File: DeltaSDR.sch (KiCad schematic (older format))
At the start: 48 parts, among them J1 Conn_01x03_Male, J2 Conn_01x05_Male, J3 Barrel_Jack, J4 USB_A, U1 TC1262-33, U2 Si570, U4 PCM3060, U5 CY8C3246PVI-147, U6 TLV761, U7 TLV761, U8 74HC74, Y1 Crystal

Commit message: Added RF front end and LNA
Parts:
- C1, C10, C11, C12, C13, C14, C15, C16, C17, C18, C19, C2, C20, C21, C22, C23, C24, C3, C4, C5, C6, C7, C8, C9: symbol DeltaSDR-rescue:C-Device -> DeltaSDR-rescue:C-Device-DeltaSDR-rescue
- D1: symbol DeltaSDR-rescue:LED-Device -> DeltaSDR-rescue:LED-Device-DeltaSDR-rescue
- D2: symbol device:D -> DeltaSDR-rescue:D-device
- D3: symbol ESD_Protection:PRTR5V0U2X -> DeltaSDR-rescue:PRTR5V0U2X-ESD_Protection
- J3: symbol Connector:Barrel_Jack -> DeltaSDR-rescue:Barrel_Jack-Connector
- L1: symbol device:L -> DeltaSDR-rescue:L-device
- R1, R2, R3, R4, R5, R6, R7, R8: symbol DeltaSDR-rescue:R-Device -> DeltaSDR-rescue:R-Device-DeltaSDR-rescue
- U1: symbol regul:TC1262-33 -> DeltaSDR-rescue:TC1262-33-regul
- U2: symbol DeltaSDR-rescue:Si570-Oscillator -> DeltaSDR-rescue:Si570-Oscillator-DeltaSDR-rescue
- U4: symbol DeltaSDR-rescue:PCM3060-riske-symbols -> DeltaSDR-rescue:PCM3060-riske-symbols-DeltaSDR-rescue
- U5: symbol DeltaSDR-rescue:CY8C3246PVI-147-cy8c3246pvi-147 -> DeltaSDR-rescue:CY8C3246PVI-147-cy8c3246pvi-147-DeltaSDR-rescue
- U6, U7: symbol MLAB_U:LM1117 -> DeltaSDR-rescue:LM1117-MLAB_U
- U8: symbol Logic_74xx:74HC74 -> DeltaSDR-rescue:74HC74-Logic_74xx
- Y1: symbol DeltaSDR-rescue:Crystal-Device -> DeltaSDR-rescue:Crystal-Device-DeltaSDR-rescue
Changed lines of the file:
@@
 EESchema Schematic File Version 4
-EELAYER 30 0
+LIBS:DeltaSDR-cache
+EELAYER 29 0
 EELAYER END
 $Descr A4 11693 8268
@@
 $EndDescr
 $Comp
-L DeltaSDR-rescue:Si570-Oscillator U2
+L DeltaSDR-rescue:Si570-Oscillator-DeltaSDR-rescue U2
 U 1 1 5E8B430C
 P 2000 2725
@@
 $EndComp
 $Comp
-L DeltaSDR-rescue:CY8C3246PVI-147-cy8c3246pvi-147 U5
+L DeltaSDR-rescue:CY8C3246PVI-147-cy8c3246pvi-147-DeltaSDR-rescue U5
 U 1 1 5E8B959A
 P 8100 4000
@@
 $EndComp
 $Comp
-L DeltaSDR-rescue:PCM3060-riske-symbols U4
+L DeltaSDR-rescue:PCM3060-riske-symbols-DeltaSDR-rescue U4
 U 1 1 5E8BE1D1
 P 3400 4450
@@
 $EndComp
 $Comp
-L DeltaSDR-rescue:C-Device C5
+L DeltaSDR-rescue:C-Device-DeltaSDR-rescue C5
 U 1 1 5E8BF4A8
 P 9500 3050
@@
 Connection ~ 9500 2850
 $Comp
-L DeltaSDR-rescue:C-Device C2
+L DeltaSDR-rescue:C-Device-DeltaSDR-rescue C2
 U 1 1 5E8C2E1C
 P 9100 3150
@@
 	9100 3300 9100 3350
 $Comp
-L DeltaSDR-rescue:C-Device C6
+L DeltaSDR-rescue:C-Device-DeltaSDR-rescue C6
 U 1 1 5E8C4103
 P 9700 3750
@@
 XTALo
 $Comp
-L DeltaSDR-rescue:C-Device C4
+L DeltaSDR-rescue:C-Device-DeltaSDR-rescue C4
 U 1 1 5E8C8B8E
 P 9400 4050
@@
 Vccd
 $Comp
-L DeltaSDR-rescue:C-Device C1
+L DeltaSDR-rescue:C-Device-DeltaSDR-rescue C1
 U 1 1 5E8D021E
 P 9000 4250
@@
 BOOT
 $Comp
-L DeltaSDR-rescue:C-Device C3
+L DeltaSDR-rescue:C-Device-DeltaSDR-rescue C3
 U 1 1 5E8D2DEC
 P 9200 4750
@@
 AMP
 $Comp
-L DeltaSDR-rescue:LED-Device D1
+L DeltaSDR-rescue:LED-Device-DeltaSDR-rescue D1
 U 1 1 5E8D990B
 P 7150 4550
@@
 $EndComp
 $Comp
-L DeltaSDR-rescue:R-Device R3
+L DeltaSDR-rescue:R-Device-DeltaSDR-rescue R3
 U 1 1 5E8DA7CD
 P 6700 4550
@@
 	7450 4550 7550 4550
 $Comp
-L DeltaSDR-rescue:C-Device C14
+L DeltaSDR-rescue:C-Device-DeltaSDR-rescue C14
 U 1 1 5E8DDA4D
 P 6850 4100
@@
 	7300 4550 7450 4550
 $Comp
-L DeltaSDR-rescue:C-Device C11
+L DeltaSDR-rescue:C-Device-DeltaSDR-rescue C11
 U 1 1 5E8E3DCC
 P 6550 3850
@@
 LRCK1
 $Comp
-L DeltaSDR-rescue:C-Device C13
+L DeltaSDR-rescue:C-Device-DeltaSDR-rescue C13
 U 1 1 5E8F24C0
 P 6850 3200
@@
 BCK1
 $Comp
-L DeltaSDR-rescue:C-Device C9
+L DeltaSDR-rescue:C-Device-DeltaSDR-rescue C9
 U 1 1 5E8FBE37
 P 4650 4400
@@
 SCL
 $Comp
-L DeltaSDR-rescue:C-Device C8
+L DeltaSDR-rescue:C-Device-DeltaSDR-rescue C8
 U 1 1 5E915664
 P 2050 4600
@@
 Connection ~ 2050 4400
 $Comp
-L DeltaSDR-rescue:R-Device R1
+L DeltaSDR-rescue:R-Device-DeltaSDR-rescue R1
 U 1 1 5E93592F
 P 4450 7100
@@
 $EndComp
 $Comp
-L DeltaSDR-rescue:R-Device R2
+L DeltaSDR-rescue:R-Device-DeltaSDR-rescue R2
 U 1 1 5E935C48
 P 4800 7100
@@
 BOOT jumper \n1-2 enables USB bootloader.\n2-3 for normal operation
 $Comp
-L DeltaSDR-rescue:Crystal-Device Y1
+L DeltaSDR-rescue:Crystal-Device-DeltaSDR-rescue Y1
 U 1 1 5E94EC07
 P 6550 5200
@@
 $EndComp
 $Comp
-L DeltaSDR-rescue:C-Device C10
+L DeltaSDR-rescue:C-Device-DeltaSDR-rescue C10
 U 1 1 5E94F97D
 P 6300 5400
@@
 $EndComp
 $Comp
-L DeltaSDR-rescue:C-Device C12
+L DeltaSDR-rescue:C-Device-DeltaSDR-rescue C12
 U 1 1 5E950325
 P 6800 5400
@@
 NoConn ~ 2500 2825
 $Comp
-L DeltaSDR-rescue:C-Device C7
+L DeltaSDR-rescue:C-Device-DeltaSDR-rescue C7
 U 1 1 5E981D93
 P 1150 2425
@@
 $EndSheet
 $Comp
-L regul:TC1262-33 U1
+L DeltaSDR-rescue:TC1262-33-regul U1
 U 1 1 5E8E4808
 P 6675 950
@@
 $EndComp
 $Comp
-L DeltaSDR-rescue:C-Device C22
+L DeltaSDR-rescue:C-Device-DeltaSDR-rescue C22
 U 1 1 5E8E4DAA
 P 7025 1150
@@
 	7025 950  7025 1000
 $Comp
-L DeltaSDR-rescue:C-Device C21
+L DeltaSDR-rescue:C-Device-DeltaSDR-rescue C21
 U 1 1 5E8F2026
 P 6225 1150
@@
 	6225 1300 6225 1350
 $Comp
-L mdSupply:+5V #PWR0143
+L DeltaSDR-rescue:+5V-mdSupply #PWR0143
 U 1 1 5E8FB0F8
 P 6225 775
@@
 Connection ~ 7025 950
 $Comp
-L Connector:Barrel_Jack J3
+L DeltaSDR-rescue:Barrel_Jack-Connector J3
 U 1 1 5E905C03
 P 1075 1050
@@
 $EndComp
 $Comp
-L device:D D2
+L DeltaSDR-rescue:D-device D2
 U 1 1 5E907521
 P 1650 950
@@
 	1375 950  1500 950
 $Comp
-L DeltaSDR-rescue:C-Device C16
+L DeltaSDR-rescue:C-Device-DeltaSDR-rescue C16
 U 1 1 5E915B7F
 P 1825 1150
@@
 	1425 1150 1425 1325
 $Comp
-L device:L L1
+L DeltaSDR-rescue:L-device L1
 U 1 1 5E92544F
 P 2050 950
@@
 $EndComp
 $Comp
-L DeltaSDR-rescue:C-Device C15
+L DeltaSDR-rescue:C-Device-DeltaSDR-rescue C15
 U 1 1 5E925F10
 P 2275 1125
@@
 	2275 1275 2275 1325
 $Comp
-L Logic_74xx:74HC74 U8
+L DeltaSDR-rescue:74HC74-Logic_74xx U8
 U 1 1 5E9675F6
 P 3150 2725
@@
 $EndComp
 $Comp
-L Logic_74xx:74HC74 U8
+L DeltaSDR-rescue:74HC74-Logic_74xx U8
 U 2 1 5E9682AE
 P 4025 2725
@@
 $EndComp
 $Comp
-L Logic_74xx:74HC74 U8
+L DeltaSDR-rescue:74HC74-Logic_74xx U8
 U 3 1 5E9696A3
 P 5025 2625
@@
 $EndComp
 $Comp
-L DeltaSDR-rescue:C-Device C24
+L DeltaSDR-rescue:C-Device-DeltaSDR-rescue C24
 U 1 1 5E96B520
 P 5375 2625
@@
 Connection ~ 5025 3050
 $Comp
-L mdSupply:+5V #PWR0152
+L DeltaSDR-rescue:+5V-mdSupply #PWR0152
 U 1 1 5E97E791
 P 5025 2125
@@
 	2700 2725 2850 2725
 $Comp
-L mdSupply:+5V #PWR0153
+L DeltaSDR-rescue:+5V-mdSupply #PWR0153
 U 1 1 5EA064BB
 P 4200 2350
@@
 $EndComp
 $Comp
-L ESD_Protection:PRTR5V0U2X D3
+L DeltaSDR-rescue:PRTR5V0U2X-ESD_Protection D3
 U 1 1 5EA126D7
 P 2925 6075
@@
 	3225 6775 2400 6775
 $Comp
-L DeltaSDR-rescue:R-Device R8
+L DeltaSDR-rescue:R-Device-DeltaSDR-rescue R8
 U 1 1 5EA3C1AA
 P 2000 7275
@@
 	2050 7450 2000 7450
 $Comp
-L DeltaSDR-rescue:R-Device R6
+L DeltaSDR-rescue:R-Device-DeltaSDR-rescue R6
 U 1 1 5EA5D9BB
 P 3500 6675
@@
 $EndComp
 $Comp
-L DeltaSDR-rescue:R-Device R7
+L DeltaSDR-rescue:R-Device-DeltaSDR-rescue R7
 U 1 1 5EA5EDBA
 P 3500 6775
@@
 USB-
 $Comp
-L MLAB_U:LM1117 U6
+L DeltaSDR-rescue:LM1117-MLAB_U U6
 U 1 1 5EA8F70D
 P 3000 1050
@@
 	3000 1350 3000 1375
 $Comp
-L DeltaSDR-rescue:C-Device C17
+L DeltaSDR-rescue:C-Device-DeltaSDR-rescue C17
 U 1 1 5EAA8526
 P 3425 1150
@@
 $EndComp
 $Comp
-L DeltaSDR-rescue:C-Device C18
+L DeltaSDR-rescue:C-Device-DeltaSDR-rescue C18
 U 1 1 5EAA8B35
 P 3800 1150
@@
 Connection ~ 3800 950
 $Comp
-L MLAB_U:LM1117 U7
+L DeltaSDR-rescue:LM1117-MLAB_U U7
 U 1 1 5EADB5DF
 P 4700 1050
@@
 	4700 1350 4700 1375
 $Comp
-L DeltaSDR-rescue:C-Device C19
+L DeltaSDR-rescue:C-Device-DeltaSDR-rescue C19
 U 1 1 5EADB5F5
 P 5125 1150
@@
 $EndComp
 $Comp
-L DeltaSDR-rescue:C-Device C20
+L DeltaSDR-rescue:C-Device-DeltaSDR-rescue C20
 U 1 1 5EADB5FF
 P 5500 1150
@@
 	5500 1300 5500 1375
 $Comp
-L DeltaSDR-rescue:C-Device C23
+L DeltaSDR-rescue:C-Device-DeltaSDR-rescue C23
 U 1 1 5EAED66B
 P 4225 1175
@@
 	2550 950  2600 950
 $Comp
-L mdSupply:+5V #PWR0164
+L DeltaSDR-rescue:+5V-mdSupply #PWR0164
 U 1 1 5EB17953
 P 5500 850
@@
 Connection ~ 5500 950
 $Comp
-L DeltaSDR-rescue:R-Device R5
+L DeltaSDR-rescue:R-Device-DeltaSDR-rescue R5
 U 1 1 5EB28564
 P 2300 5975
@@
 $EndComp
 $Comp
-L DeltaSDR-rescue:R-Device R4
+L DeltaSDR-rescue:R-Device-DeltaSDR-rescue R4
 U 1 1 5EB28C53
 P 1950 5975
@@
 	2075 5850 2125 5850
 $Comp
-L mdSupply:+12V #PWR0166
+L DeltaSDR-rescue:+12V-mdSupply #PWR0166
 U 1 1 5EB743BC
 P 2400 850

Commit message: First layouting
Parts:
- removed Y1: Crystal, symbol DeltaSDR-rescue:Crystal-Device-DeltaSDR-rescue
- added Y1: Crystal_GND24, Crystal:Crystal_SMD_3225-4Pin_3.2x2.5mm, symbol Device:Crystal_GND24
- D1: footprint (none) -> LED_SMD:LED_0805_2012Metric
- D2: footprint (none) -> Diode_SMD:D_SMC
- D3: footprint (none) -> Package_TO_SOT_SMD:SOT-143
- J1: footprint (none) -> Connector_PinHeader_2.54mm:PinHeader_1x03_P2.54mm_Vertical
- J2: footprint (none) -> Connector_PinHeader_2.54mm:PinHeader_1x05_P2.54mm_Vertical
- J3: footprint (none) -> Connector_BarrelJack:BarrelJack_Horizontal
- J4: footprint (none) -> Connector_USB:USB_B_TE_5787834_Vertical
- L1: footprint (none) -> Inductor_SMD:L_0805_2012Metric
- U8: footprint (none) -> Package_SO:SOIC-14_3.9x8.7mm_P1.27mm
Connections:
- net GND: now also Y1.2, Y1.4
- net XTALi: now also Y1.1
- net XTALo: now also Y1.3
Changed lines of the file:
@@
 F 0 "D1" H 7143 4295 50  0000 C CNN
 F 1 "LED" H 7143 4386 50  0000 C CNN
-F 2 "" H 7150 4550 50  0001 C CNN
+F 2 "LED_SMD:LED_0805_2012Metric" H 7150 4550 50  0001 C CNN
 F 3 "~" H 7150 4550 50  0001 C CNN
 	1    7150 4550
@@
 F 0 "J1" V 4762 5762 50  0000 R CNN
 F 1 "Conn_01x03_Male" V 4853 5762 50  0000 R CNN
-F 2 "" H 4700 5950 50  0001 C CNN
+F 2 "Connector_PinHeader_2.54mm:PinHeader_1x03_P2.54mm_Vertical" H 4700 5950 50  0001 C CNN
 F 3 "~" H 4700 5950 50  0001 C CNN
 	1    4700 5950
@@
 BOOT jumper \n1-2 enables USB bootloader.\n2-3 for normal operation
 $Comp
-L DeltaSDR-rescue:Crystal-Device-DeltaSDR-rescue Y1
-U 1 1 5E94EC07
-P 6550 5200
-F 0 "Y1" H 6550 5468 50  0000 C CNN
-F 1 "Crystal" H 6550 5377 50  0000 C CNN
-F 2 "" H 6550 5200 50  0001 C CNN
-F 3 "~" H 6550 5200 50  0001 C CNN
-	1    6550 5200
-	1    0    0    -1
-$EndComp
-$Comp
 L DeltaSDR-rescue:C-Device-DeltaSDR-rescue C10
 U 1 1 5E94F97D
 P 6300 5400
-F 0 "C10" H 6415 5446 50  0000 L CNN
-F 1 "22p" H 6415 5355 50  0000 L CNN
+F 0 "C10" H 6050 5450 50  0000 L CNN
+F 1 "22p" H 6050 5350 50  0000 L CNN
 F 2 "Capacitor_SMD:C_0603_1608Metric" H 6338 5250 50  0001 C CNN
 F 3 "~" H 6300 5400 50  0001 C CNN
@@
 F 0 "J2" H 6122 6782 50  0000 R CNN
 F 1 "Conn_01x05_Male" H 6122 6873 50  0000 R CNN
-F 2 "" H 6150 6850 50  0001 C CNN
+F 2 "Connector_PinHeader_2.54mm:PinHeader_1x05_P2.54mm_Vertical" H 6150 6850 50  0001 C CNN
 F 3 "~" H 6150 6850 50  0001 C CNN
 	1    6150 6850
@@
 F 0 "J3" H 1154 1375 50  0000 C CNN
 F 1 "Barrel_Jack" H 1154 1284 50  0000 C CNN
-F 2 "" H 1125 1010 50  0001 C CNN
+F 2 "Connector_BarrelJack:BarrelJack_Horizontal" H 1125 1010 50  0001 C CNN
 F 3 "~" H 1125 1010 50  0001 C CNN
 	1    1075 1050
@@
 F 0 "D2" H 1650 734 50  0000 C CNN
 F 1 "D" H 1650 825 50  0000 C CNN
-F 2 "" H 1650 950 50  0001 C CNN
+F 2 "Diode_SMD:D_SMC" H 1650 950 50  0001 C CNN
 F 3 "" H 1650 950 50  0001 C CNN
 	1    1650 950
@@
 F 0 "L1" V 2240 950 50  0000 C CNN
 F 1 "74279220321" V 2149 950 50  0000 C CNN
-F 2 "" H 2050 950 50  0001 C CNN
+F 2 "Inductor_SMD:L_0805_2012Metric" H 2050 950 50  0001 C CNN
 F 3 "" H 2050 950 50  0001 C CNN
 	1    2050 950
@@
 F 0 "U8" H 3000 2975 50  0000 C CNN
 F 1 "74HC74" H 3325 2475 50  0000 C CNN
-F 2 "" H 3150 2725 50  0001 C CNN
+F 2 "Package_SO:SOIC-14_3.9x8.7mm_P1.27mm" H 3150 2725 50  0001 C CNN
 F 3 "74xx/74hc_hct74.pdf" H 3150 2725 50  0001 C CNN
 	1    3150 2725
@@
 F 0 "U8" H 3875 2975 50  0000 C CNN
 F 1 "74HC74" H 4200 2475 50  0000 C CNN
-F 2 "" H 4025 2725 50  0001 C CNN
+F 2 "Package_SO:SOIC-14_3.9x8.7mm_P1.27mm" H 4025 2725 50  0001 C CNN
 F 3 "74xx/74hc_hct74.pdf" H 4025 2725 50  0001 C CNN
 	2    4025 2725
@@
 F 0 "U8" H 4800 2975 50  0000 L CNN
 F 1 "74HC74" H 5075 2250 50  0000 L CNN
-F 2 "" H 5025 2625 50  0001 C CNN
+F 2 "Package_SO:SOIC-14_3.9x8.7mm_P1.27mm" H 5025 2625 50  0001 C CNN
 F 3 "74xx/74hc_hct74.pdf" H 5025 2625 50  0001 C CNN
 	3    5025 2625
@@
 F 0 "J4" H 2157 7142 50  0000 C CNN
 F 1 "USB_A" H 2157 7051 50  0000 C CNN
-F 2 "" H 2250 6625 50  0001 C CNN
+F 2 "Connector_USB:USB_B_TE_5787834_Vertical" H 2250 6625 50  0001 C CNN
 F 3 "" H 2250 6625 50  0001 C CNN
 	1    2100 6675
@@
 F 0 "D3" H 2925 6442 50  0000 C CNN
 F 1 "PRTR5V0U2X" H 2925 6351 50  0000 C CNN
-F 2 "" H 2975 6025 50  0001 C CNN
+F 2 "Package_TO_SOT_SMD:SOT-143" H 2975 6025 50  0001 C CNN
 F 3 "https://assets.nexperia.com/documents/data-sheet/PRTR5V0U2X.pdf" H 2975 6025 50  0001 C CNN
 	1    2925 6075
@@
 Wire Wire Line
 	2400 950  2550 950
+$Comp
+L Device:Crystal_GND24 Y1
+U 1 1 5E9781A4
+P 6550 5200
+F 0 "Y1" H 6350 5350 50  0000 L CNN
+F 1 "Crystal_GND24" H 6700 5350 50  0000 L CNN
+F 2 "Crystal:Crystal_SMD_3225-4Pin_3.2x2.5mm" H 6550 5200 50  0001 C CNN
+F 3 "~" H 6550 5200 50  0001 C CNN
+	1    6550 5200
+	1    0    0    -1
+$EndComp
+$Comp
+L power:GND #PWR0221
+U 1 1 5E9783E9
+P 6550 5600
+F 0 "#PWR0221" H 6550 5350 50  0001 C CNN
+F 1 "GND" H 6555 5427 50  0000 C CNN
+F 2 "" H 6550 5600 50  0001 C CNN
+F 3 "" H 6550 5600 50  0001 C CNN
+	1    6550 5600
+	1    0    0    -1
+$EndComp
+Wire Wire Line
+	6550 5400 6550 5600
+Wire Wire Line
+	6550 5000 6550 4950
+Wire Wire Line
+	6550 4950 6000 4950
+Wire Wire Line
+	6000 4950 6000 5600
+Wire Wire Line
+	6000 5600 6300 5600
+Connection ~ 6300 5600
 $EndSCHEMATC

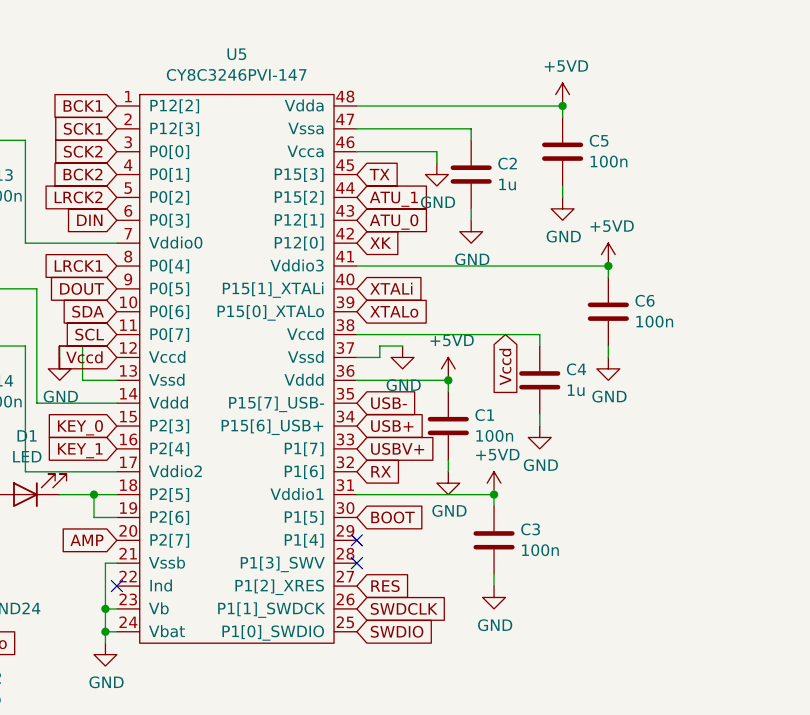
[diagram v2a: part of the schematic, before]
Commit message: Added remaining switching signals and polygons
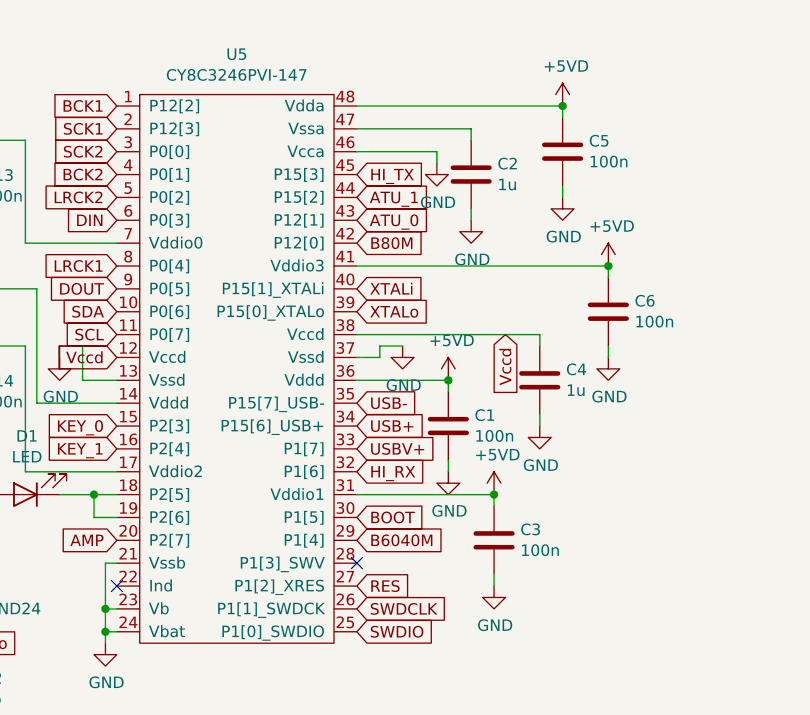
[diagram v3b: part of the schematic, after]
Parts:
- D2: footprint Diode_SMD:D_SMC -> Diode_SMD:D_SMB
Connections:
- net B6040M: now reaches U5.29 (P1[4])
- net RX renamed HI_RX
- net TX renamed HI_TX
- net XK renamed B80M
- no-connect marks 6 -> 5
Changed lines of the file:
@@
 	9500 3200 9500 3250
 Text GLabel 8600 3150 2    50   Input ~ 0
-TX
+HI_TX
 Text GLabel 8600 3250 2    50   Input ~ 0
 ATU_1
@@
 ATU_0
 Text GLabel 8600 3450 2    50   Input ~ 0
-XK
+B80M
 $Comp
 L power:+5VD #PWR0102
@@
 USBV+
 Text GLabel 8600 4450 2    50   Input ~ 0
-RX
+HI_RX
 Text GLabel 8600 4650 2    50   Input ~ 0
 BOOT
@@
 RES
 NoConn ~ 8600 4850
-NoConn ~ 8600 4750
 $Comp
 L Connector:Conn_01x05_Male J2
@@
 F 0 "D2" H 1650 734 50  0000 C CNN
 F 1 "D" H 1650 825 50  0000 C CNN
-F 2 "Diode_SMD:D_SMC" H 1650 950 50  0001 C CNN
+F 2 "Diode_SMD:D_SMB" H 1650 950 50  0001 C CNN
 F 3 "" H 1650 950 50  0001 C CNN
 	1    1650 950
@@
 	6000 5600 6300 5600
 Connection ~ 6300 5600
+Text GLabel 8600 4750 2    50   Input ~ 0
+B6040M
 $EndSCHEMATC
